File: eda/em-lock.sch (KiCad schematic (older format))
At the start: 46 parts

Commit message: refs #38128 EXTI interrupts, r/a container, iterator w/o start/end
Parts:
- added D1: M7, I20:SMA_Standard, symbol D
- added D2: ZENER-MOSFET-GATE, I20:MiniMELF_Standard, symbol ZENER
- added D3: D_Schottky, I20:SMA_Standard, symbol D_Schottky
- added P2: BTN_CALL, I20:JST_XH_B02B-XH-A_02x2.50mm_Straight, symbol CONN_01X02
- added P4: LOCK_CONN, I20:PhoenixContact_MSTBA-G_04x5.08mm_Angled, symbol CONN_01X04
- added P6: PWR_SW_CONN, I20:JST_XH_B02B-XH-A_02x2.50mm_Straight, symbol CONN_01X02
- added Q1: Q_NMOS_DGS, I20:SOT-23, symbol Q_NMOS_DGS
- added R2, R5: 10k, I20:R_0805, symbol R
- added R7: 240, I20:R_0805, symbol R
- added U1: 74LVC2G14, I20:SOT-23-6, symbol 74LVC2G14
- C1, C10, C11, C12, C13, C14, C2, C3, C4, C5, C6, C7, C8, C9: renamed from C?; footprint (none) -> I20:C_0805_HandSoldering
- CON1: renamed from CON?; footprint (none) -> I20:DC-005
- D4: renamed from D?; value 12V -> LDO-12V; footprint (none) -> I20:Fuse_SMD1206_Wave
- D5: renamed from D?; footprint (none) -> I20:LED-RGB-5MM_Common_Cathode
- F1: renamed from F?; footprint (none) -> I20:Fuse_SMD1206_Wave
- P1: renamed from P?; value CONN_01X02 -> BTN_OPEN; footprint (none) -> I20:JST_XH_B02B-XH-A_02x2.50mm_Straight
- P10: renamed from P?; value CONN_01X04 -> EXT_LED_CONN; footprint (none) -> I20:JST_XH_B04B-XH-A_04x2.50mm_Straight
- P3: renamed from P?; value CONN_02X03 -> BOOT_SEL_CONN; footprint (none) -> I20:Pin_Header_Straight_2x03
- P5: renamed from P?; value CONN_01X03 -> PWR_SELECT; footprint (none) -> I20:Pin_Header_Straight_1x03
- P7: renamed from P?; value CONN_01X04 -> SWD_CONN; footprint (none) -> I20:Pin_Header_Straight_1x04
- P8: renamed from P?; value CONN_02X04 -> ESP8266_CONN; footprint (none) -> I20:ESP8266_CONN
- P9: renamed from P?; footprint (none) -> I20:conn_usb_B_micro_smd-2
- Q2, Q3, Q4: renamed from Q?; footprint SOT-23 -> I20:SOT-23
- R1, R10, R11, R12, R13, R14, R15, R16, R17, R3, R4, R6, R8, R9: renamed from R?; footprint (none) -> I20:R_0805
- SW1: renamed from SW?; value SW_PUSH -> RST_BTN; footprint (none) -> I20:SW_SPST_B3U-1000P
- U2: renamed from U?; footprint LQFP48 -> I20:SparkFun-LQFP-48
- U3: renamed from U?; footprint SOT-223 -> I20:SOT-223
- Y1: renamed from Y?; footprint (none) -> I20:Crystal_HC49-U_Vertical
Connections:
- net labels added: 12V_EXT, 5V_USB, BOOT0, BOOT1, BTN_CALL, BTN_OPEN, EM_LOCK, LDO_IN, LOCK_GND, LOCK_OPEN, NRST, OSC_IN, OSC_OUT, PIN_BLUE, PIN_GREEN, PIN_RED, PWR_UNFUSED, UART_EXT_RX, UART_EXT_TX, UART_INT_RX, UART_INT_TX, VBAT, VCC
- net labels removed: +12V
- wire segments 193 -> 187
- no-connect marks 0 -> 20
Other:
- moved on the sheet: C3, C4, CON1, P1, P3, P5, R1, R3, R4, R8, SW1

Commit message: refs #39740 double mode_change fix, authorization implemented.
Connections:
- net labels added: ESP_RESET
- wire segments 187 -> 189
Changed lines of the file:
@@
 Text Label 7550 8000 0    60   ~ 0
 UART_EXT_RX
+Wire Wire Line
+	13950 7700 15800 7700
+Wire Wire Line
+	15800 7700 15800 7900
+Text Label 14300 7700 0    60   ~ 0
+ESP_RESET
 $EndSCHEMATC

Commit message: refs #41563 implemented kicad schematics stm32 hierarchical sheet.
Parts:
- removed C1, C2: 2pF, I20:C_0805_HandSoldering, symbol C
- removed C10: 1uF, I20:C_0805_HandSoldering, symbol C
- removed C11, C9: 10uF, I20:C_0805_HandSoldering, symbol C
- removed C12: 22uF, I20:C_0805_HandSoldering, symbol C
- removed C3, C4, C5, C6, C7, C8: 100nF, I20:C_0805_HandSoldering, symbol C
- removed CON1: BARREL_JACK, I20:DC-005, symbol BARREL_JACK
- removed D3: D_Schottky, I20:SMA_Standard, symbol D_Schottky
- removed D4: LDO-12V, I20:Fuse_SMD1206_Wave, symbol ZENER
- removed F1: F_Small, I20:Fuse_SMD1206_Wave, symbol F_Small
- removed P3: BOOT_SEL_CONN, I20:Pin_Header_Straight_2x03, symbol CONN_02X03
- removed P5: PWR_SELECT, I20:Pin_Header_Straight_1x03, symbol CONN_01X03
- removed P6: PWR_SW_CONN, I20:JST_XH_B02B-XH-A_02x2.50mm_Straight, symbol CONN_01X02
- removed P7: SWD_CONN, I20:Pin_Header_Straight_1x04, symbol CONN_01X04
- removed P9: USB_B, I20:conn_usb_B_micro_smd-2, symbol USB_B
- removed R3, R4, R8: 10k, I20:R_0805, symbol R
- removed R6: 0R, I20:R_0805, symbol R
- removed SW1: RST_BTN, I20:SW_SPST_B3U-1000P, symbol SW_PUSH
- removed U2: STM32F103C8Tx, I20:SparkFun-LQFP-48, symbol STM32F103C8Tx
- removed U3: LD1117S33CTR, I20:SOT-223, symbol LD1117S33CTR
- removed Y1: 8MHz, I20:Crystal_HC49-U_Vertical, symbol Crystal
- renumbered C13 to C?, C14 to C?, D5 to D?, D2 to D?, D1 to D?, P10 to P?, P4 to P?, P2 to P?, P8 to P?, P1 to P?, Q2 to Q?, Q3 to Q?, Q4 to Q?, Q1 to Q?, R12 to R?, R13 to R?, R14 to R?, R9 to R?, R10 to R?, R11 to R?, R7 to R?, R15 to R?, R16 to R?, R17 to R?, R5 to R?, R1 to R?, R2 to R?, U1 to U?
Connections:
- net labels removed: +5V, 12V_EXT, 5V_USB, BOOT0, BOOT1, LDO_IN, NRST, OSC_IN, OSC_OUT, PWR_UNFUSED, VBAT, VCC
- wire segments 189 -> 73
- no-connect marks 20 -> 0
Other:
- note added: "CPU + periph"
- note added: "Call button"
- note added: "ESP8266 connector"
- note added: "Em-lock connector"
- note added: "Open button"
- note added: "RGB LED connector/placement"
- moved on the sheet: C?, D?, P?, Q?, R?, U?A

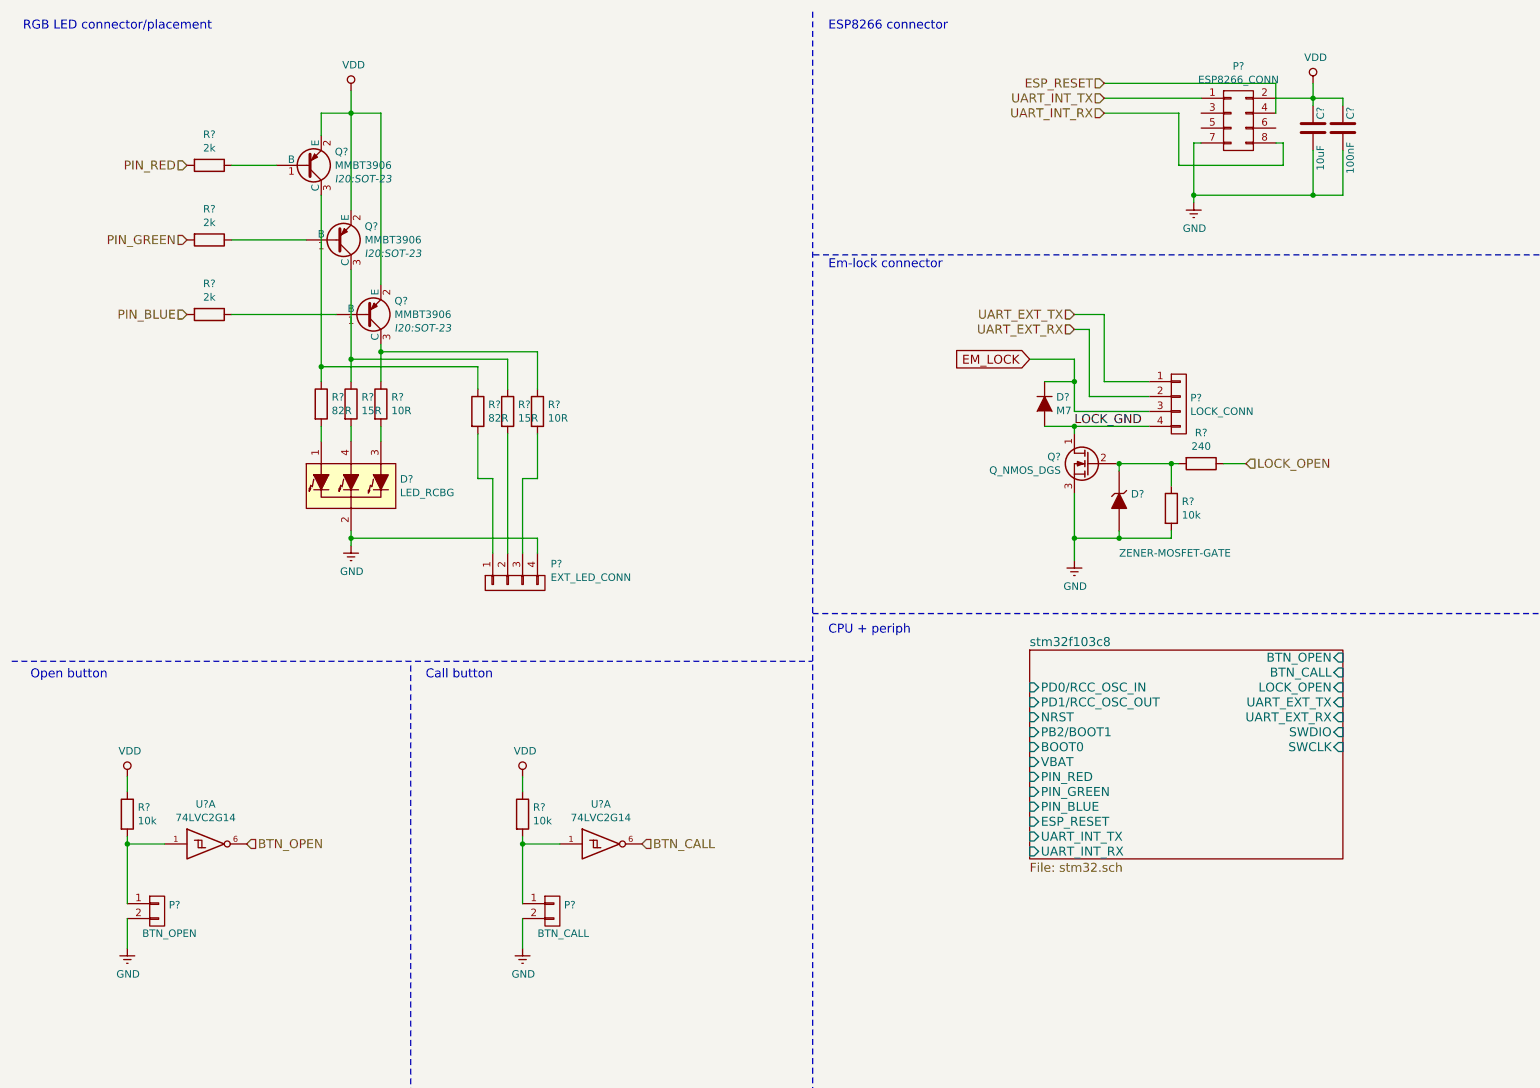
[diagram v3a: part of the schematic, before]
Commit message: refs #41563 update kicad schematics stm32 hierarchical sheet.
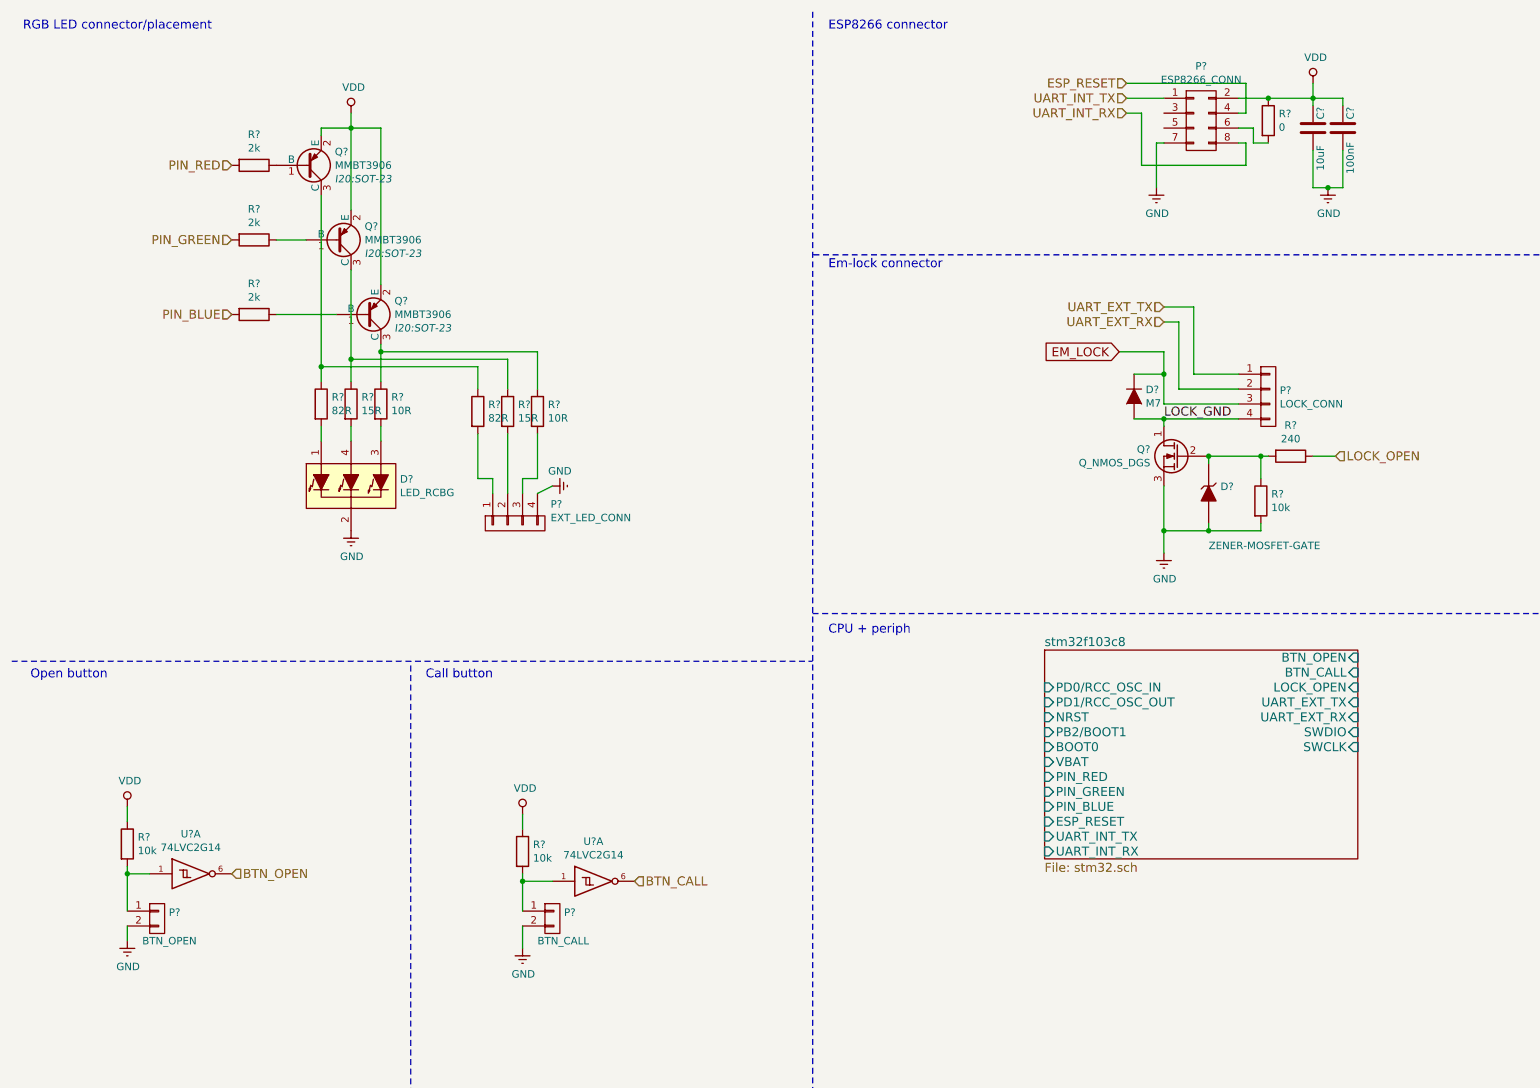
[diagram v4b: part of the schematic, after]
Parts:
- added R?: 0, I20:R_0805, symbol R
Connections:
- net VDD: now also R?.1
- net at P?.6 (P6): now also R?.2
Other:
- moved on the sheet: D?, P?, Q?, R?, U?A

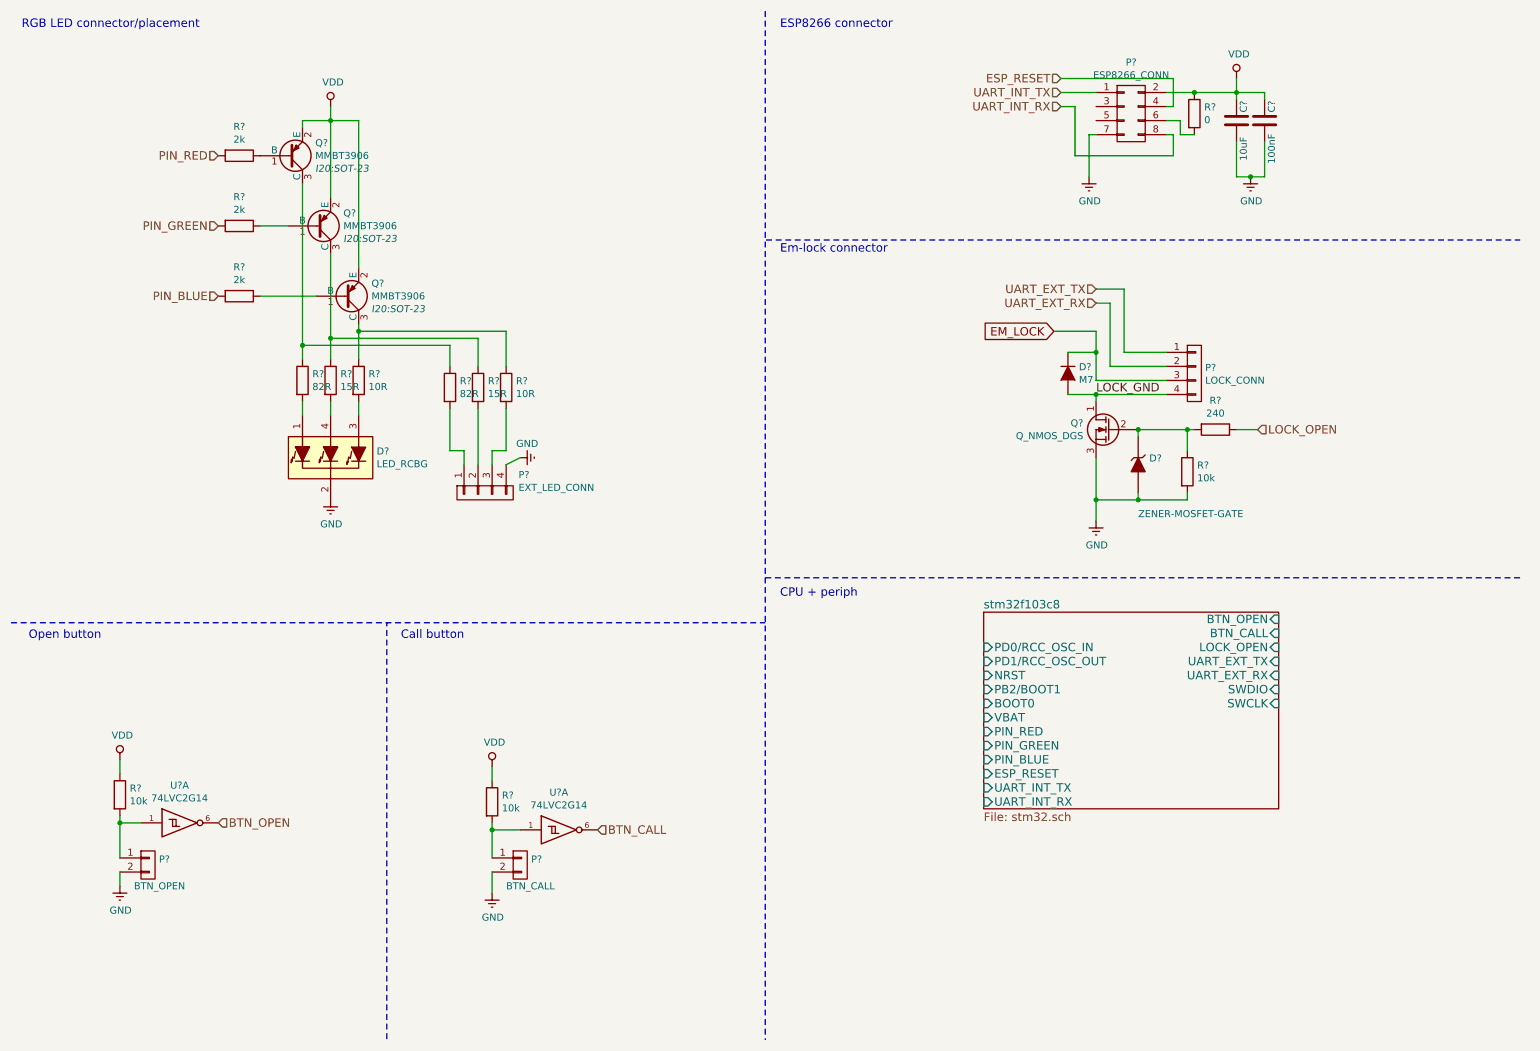
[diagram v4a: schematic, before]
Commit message: refs #41563 refined em-lock schematics, 2 spi rc522 devices added.
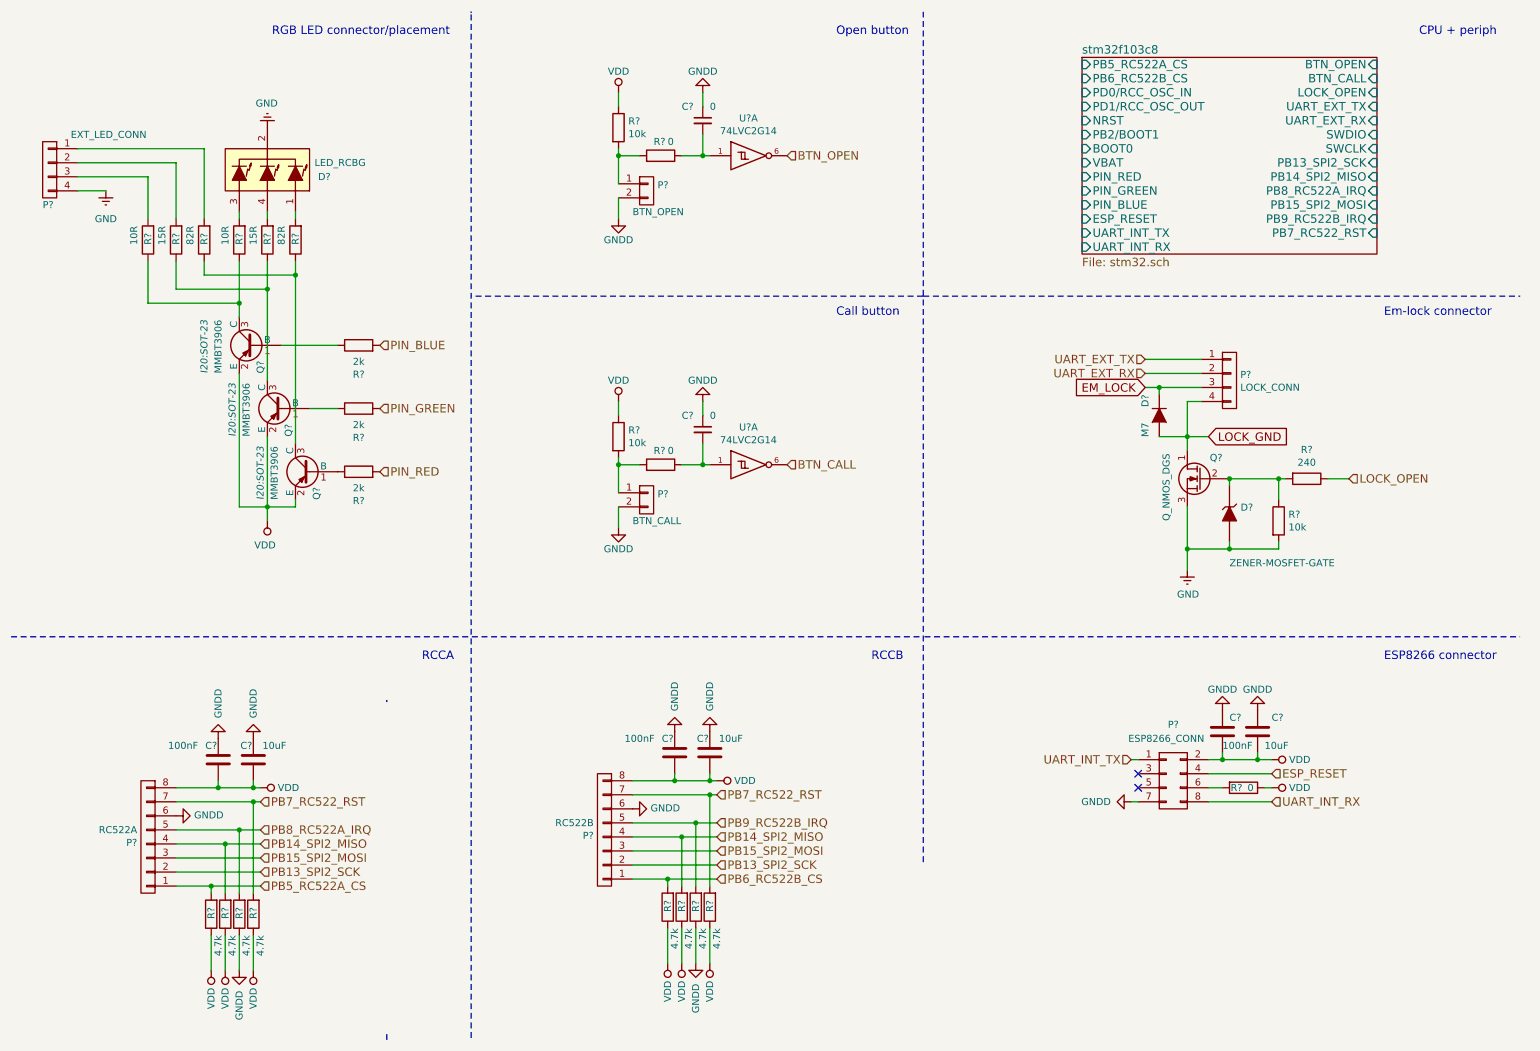
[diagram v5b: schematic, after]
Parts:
- removed P?: BTN_OPEN, I20:JST_XH_B02B-XH-A_02x2.50mm_Straight, symbol CONN_01X02
- removed R?: 10k, I20:R_0805, symbol R
- removed U?: 74LVC2G14, I20:SOT-23-6, symbol 74LVC2G14
- added C? (x2): 10uF, I20:C_0805_HandSoldering, symbol C
- added C? (x2): 100nF, I20:C_0805_HandSoldering, symbol C
- added C? (x2): 0, symbol C_Small
- added P?: RC522A, symbol CONN_01X08
- added P?: BTN_OPEN, I20:JST_XH_B02B-XH-A_02x2.50mm_Straight, symbol CONN_01X02
- added P?: RC522B, symbol CONN_01X08
- added R? (x8): 4.7k, I20:R_0805, symbol R
- added R? (x2): 0, I20:R_0805, symbol R
- added R?: 10k, I20:R_0805, symbol R
- added U?: 74LVC2G14, I20:SOT-23-6, symbol 74LVC2G14
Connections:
- net BTN_OPEN: now also U?.6
- net GND: now also U?.2 (GND)
- net GNDREF: no longer C?.1, C?.1, P?.2 (P2), P?.7 (P7)
- net VCC: now also U?.5 (VCC)
- net VDD: now also C?.1, C?.1, C?.1, C?.1, P?.8 (P8), P?.8 (P8), R?.1, R?.1, R?.1, R?.1, R?.1, R?.1, R?.1
- net at P?.1 (P1), R?.2: now also R?.2; no longer U?.1
- new net: C?.2, R?.1, U?.1 (x2)
- new net: P?.1 (P1), R?.2, R?.2
- new net GNDD: C?.1, C?.1, C?.1, C?.1, C?.2, C?.2, C?.2, C?.2, P?.2 (P2), P?.2 (P2), P?.6 (P6), P?.6 (P6), P?.7 (P7), R?.1, R?.1
- new net PB13_SPI2_SCK: P?.2 (P2), P?.2 (P2)
- new net PB14_SPI2_MISO: P?.4 (P4), P?.4 (P4), R?.2, R?.2
- new net PB15_SPI2_MOSI: P?.3 (P3), P?.3 (P3)
- new net PB5_RC522A_CS: P?.1 (P1), R?.2
- new net PB6_RC522B_CS: P?.1 (P1), R?.2
- new net PB7_RC522_RST: P?.7 (P7), P?.7 (P7), R?.2, R?.2
- new net PB8_RC522A_IRQ: P?.5 (P5), R?.2
- new net PB9_RC522B_IRQ: P?.5 (P5), R?.2
- no-connect marks 0 -> 2
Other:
- note added: "RCCA"
- note added: "RCCB"
- moved on the sheet: C?, D?, P?, Q?, R?, U?A
